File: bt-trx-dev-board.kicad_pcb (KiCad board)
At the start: 2 copper layers, 78 x 68 mm, 54 parts, among them J1 RJ45, J2 PTT_BUTTON, J3 AudioJack3, J4 ENAPLE_PTT_PULLUP, J5 PTT_SELECT, J6 I2C, J7 Conn_01x02, SW1 SW_Push, U1 SILabs_WT32i, U3 ESP32-DEVKIT

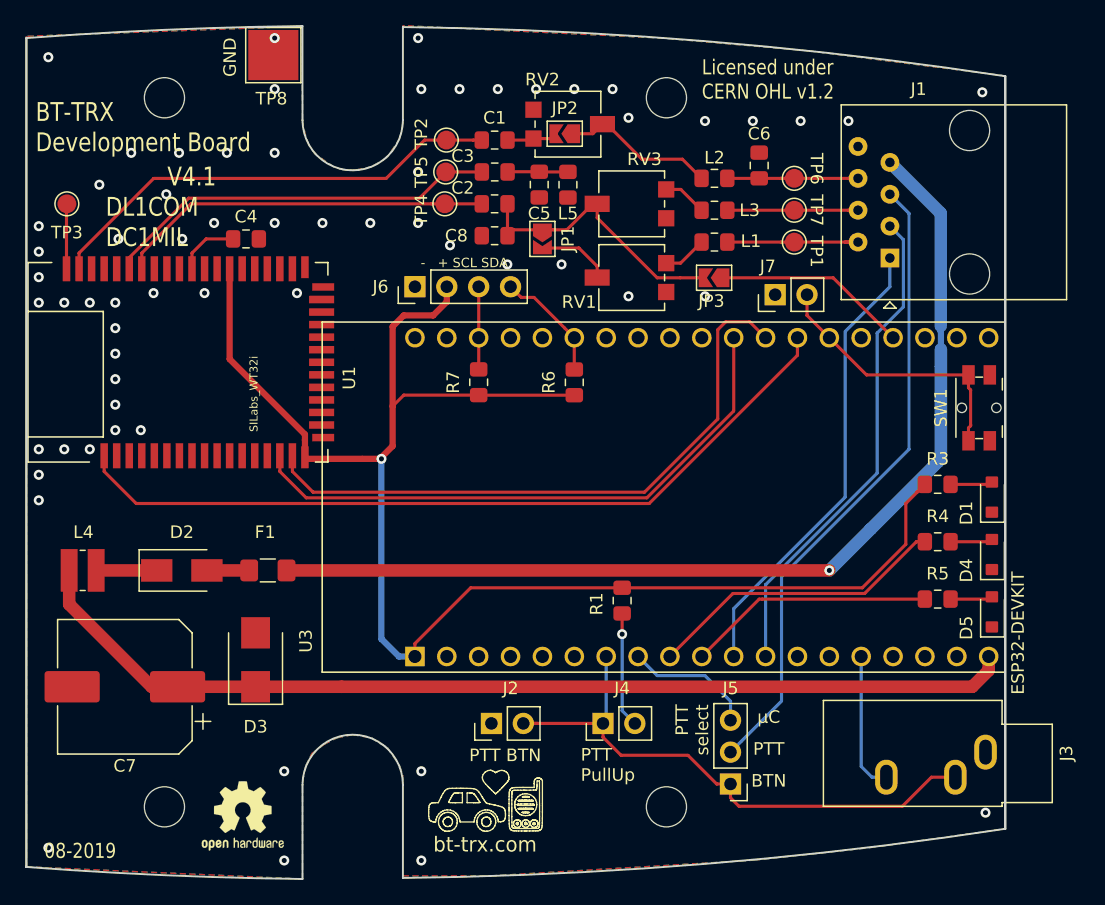
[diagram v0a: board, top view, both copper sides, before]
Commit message: Changed Silkscreen a bit
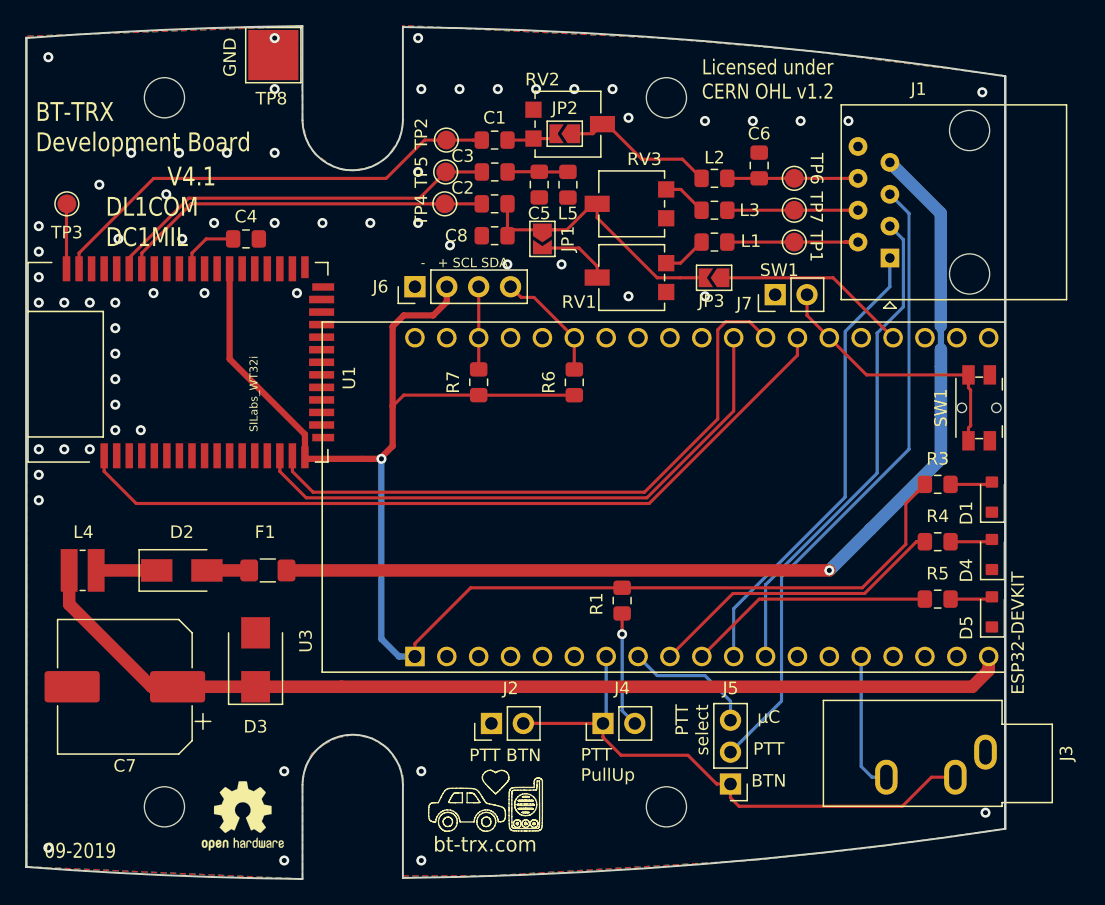
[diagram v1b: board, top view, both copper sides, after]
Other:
- board text added: "09-2019"
- board text added: "SW1"
- board text removed: "08-2019"
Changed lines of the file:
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@@
   (general
     (thickness 1.6)
-    (drawings 876)
+    (drawings 877)
     (tracks 275)
     (zones 0)
@@
     (tags "test point SMD pad")
     (attr virtual)
-    (fp_text reference TP1 (at 1.778 0.762 270 unlocked) (layer F.SilkS)
+    (fp_text reference TP1 (at 1.7526 0.3302 270 unlocked) (layer F.SilkS)
       (effects (font (size 1 1) (thickness 0.15)))
     )
@@
     (tags "test point SMD pad")
     (attr virtual)
-    (fp_text reference TP7 (at 1.778 0 270 unlocked) (layer F.SilkS)
+    (fp_text reference TP7 (at 1.7526 -0.2286 270 unlocked) (layer F.SilkS)
       (effects (font (size 1 1) (thickness 0.15)))
     )
@@
     (descr "Through hole straight pin header, 1x02, 2.54mm pitch, single row")
     (tags "Through hole pin header THT 1x02 2.54mm single row")
-    (fp_text reference J7 (at 2.2606 -0.5842 180) (layer F.SilkS)
+    (fp_text reference J7 (at -0.7112 -2.4638 180) (layer F.SilkS)
       (effects (font (size 1 1) (thickness 0.15)))
     )
@@
       ))
   )
+  (gr_text SW1 (at 178.8668 84.7852) (layer F.SilkS)
+    (effects (font (size 1 1) (thickness 0.15)) (justify left))
+  )
   (gr_text "-   + SCL SDA" (at 155.321 84.201) (layer F.SilkS)
     (effects (font (size 0.75 0.75) (thickness 0.125)))
@@
   (gr_line (start 154.4549 128.13161) (end 154.550279 128.21612) (layer F.SilkS) (width 0.09))
   (gr_line (start 153.416 128.27) (end 153.456692 128.22767) (layer F.SilkS) (width 0.09))
-  (gr_text 08-2019 (at 124.714 131.064) (layer F.SilkS)
+  (gr_text 09-2019 (at 124.714 131.064) (layer F.SilkS)
     (effects (font (size 1.2 1) (thickness 0.15)))
   )

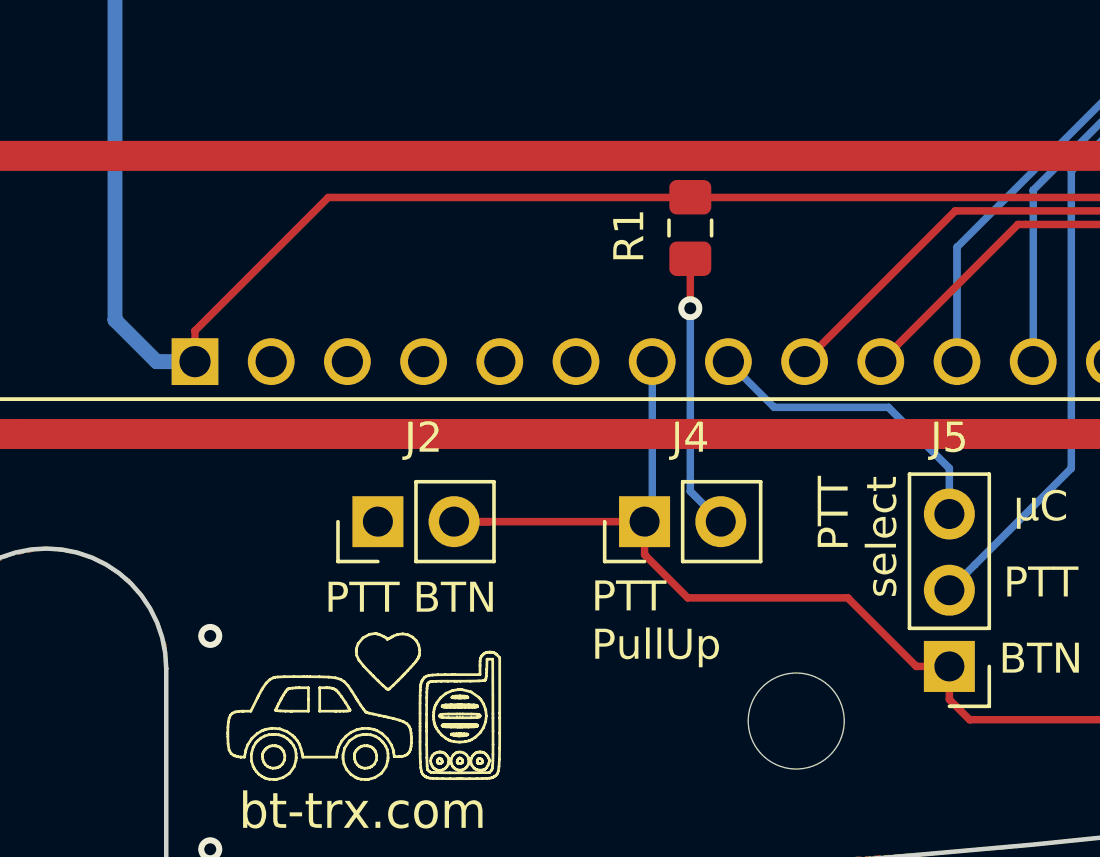
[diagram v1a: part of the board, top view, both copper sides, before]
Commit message: [#15] Replaced PTT Pullup Jumper wit Solder Jumper
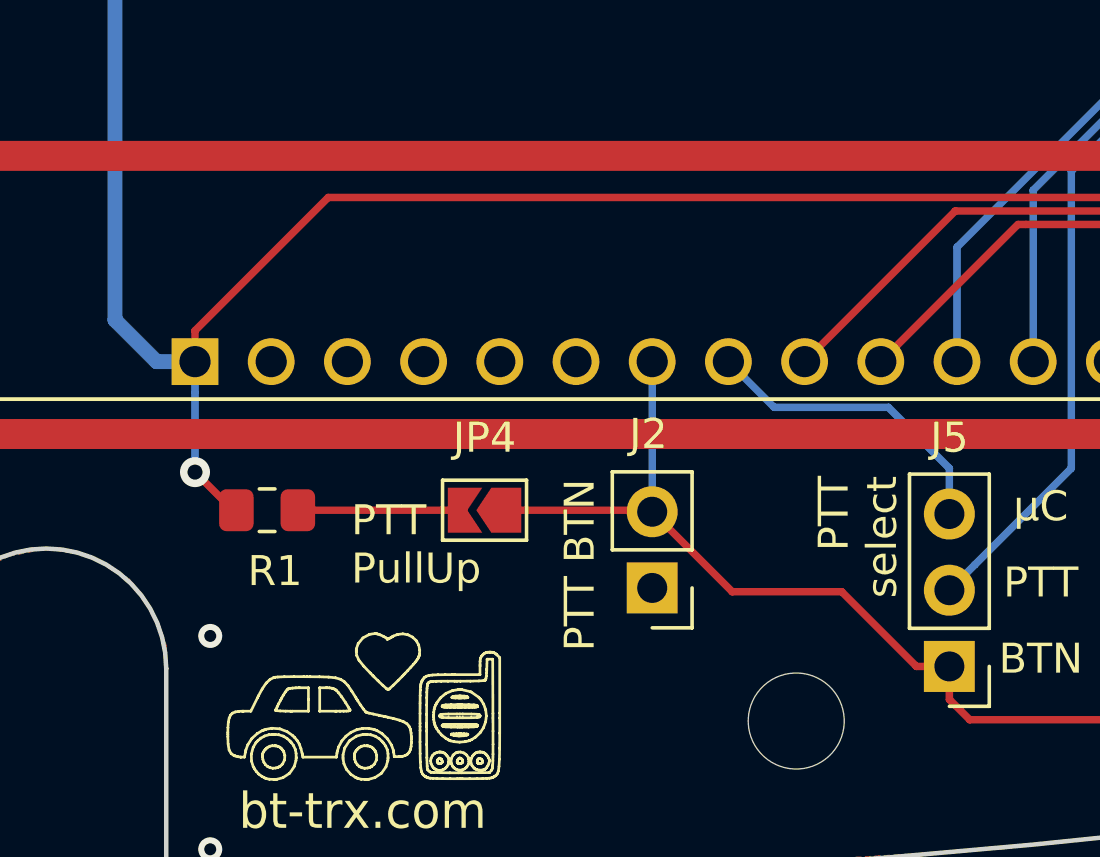
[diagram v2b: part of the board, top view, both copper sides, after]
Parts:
- removed J4: ENAPLE_PTT_PULLUP, Connector_PinHeader_2.54mm:PinHeader_1x02_P2.54mm_Vertical
- added JP4: EN_PTT_PULLUP, Jumper:SolderJumper-2_P1.3mm_Open_TrianglePad1.0x1.5mm, F.Cu at (161.0, 120.5)
- moved R1 17.0 mm to (153.8, 120.5), turned to 0 degrees
- moved J2 9.41 mm to (166.6, 123.1), turned to 180 degrees
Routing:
- net +3V3: track 122.1 -> 127.7 mm, vias 1 -> 2
- net /PTT_BUTTON: track 46.5 -> 42.2 mm
- net Net-(JP4-Pad2): track 9.18 -> 5.46 mm, vias 1 -> 0

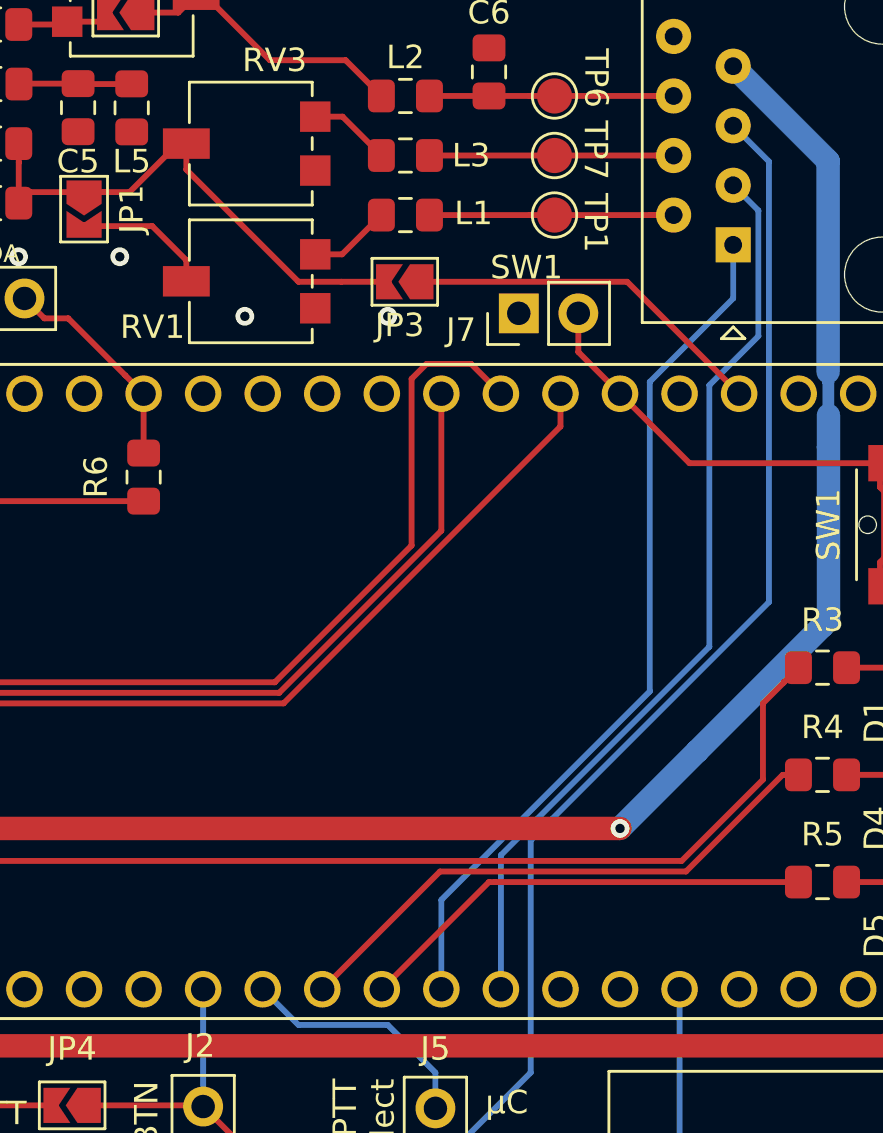
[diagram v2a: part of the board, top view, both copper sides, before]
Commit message: [#16] Move SW1 and VOX to usable Pins
* Moved SW1 form GPIO0 to GPIO18
* Added Pullup to SW1
* Moved VOX form GPIO2 to GPIO35
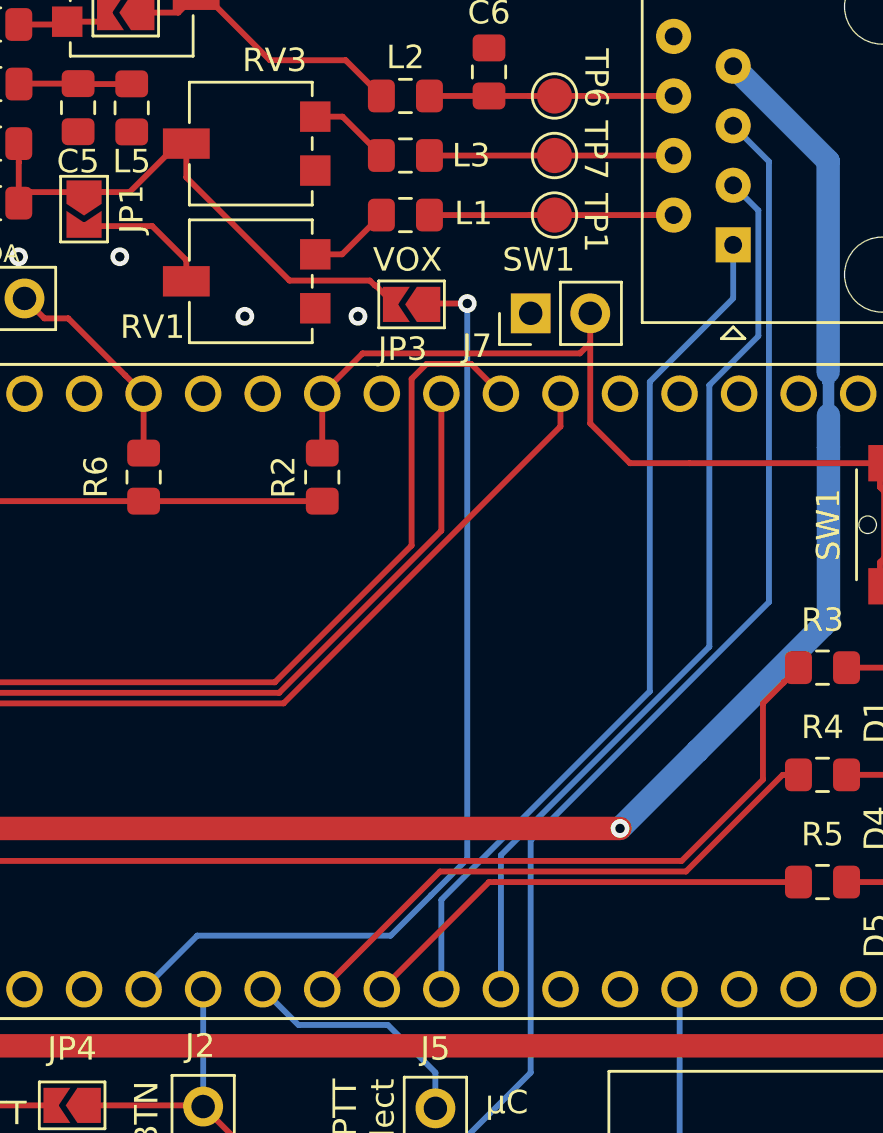
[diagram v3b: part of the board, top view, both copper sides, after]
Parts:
- added R2: 10k, Resistor_SMD:R_0805_2012Metric_Pad1.15x1.40mm_HandSolder, F.Cu at (171.7, 93.7)
- moved JP3 1.01 mm to (175.5, 86.4)
- moved J7 0.51 mm to (180.6, 86.7)
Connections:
- JP3 pad 1: Net-(JP3-Pad1) -> /Microcontroller/VOX
- U3 pad 28: (no net) -> /Microcontroller/BTN0
- U3 pad 33: /Microcontroller/BTN0 -> (no net)
- U3 pad 35: Net-(JP3-Pad1) -> (no net)
- U3 pad 6: (no net) -> /Microcontroller/VOX
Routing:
- net /Microcontroller/VOX: track 0.00 -> 41.5 mm, vias 0 -> 1
- net /Microcontroller/BTN0: track 21.6 -> 37.8 mm
- net Net-(JP3-Pad1): track 15.5 -> 0.00 mm
- net +3V3: track 127.7 -> 135.3 mm
- net AUDIO_B: track 22.4 -> 23.3 mm
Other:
- board text added: "VOX"

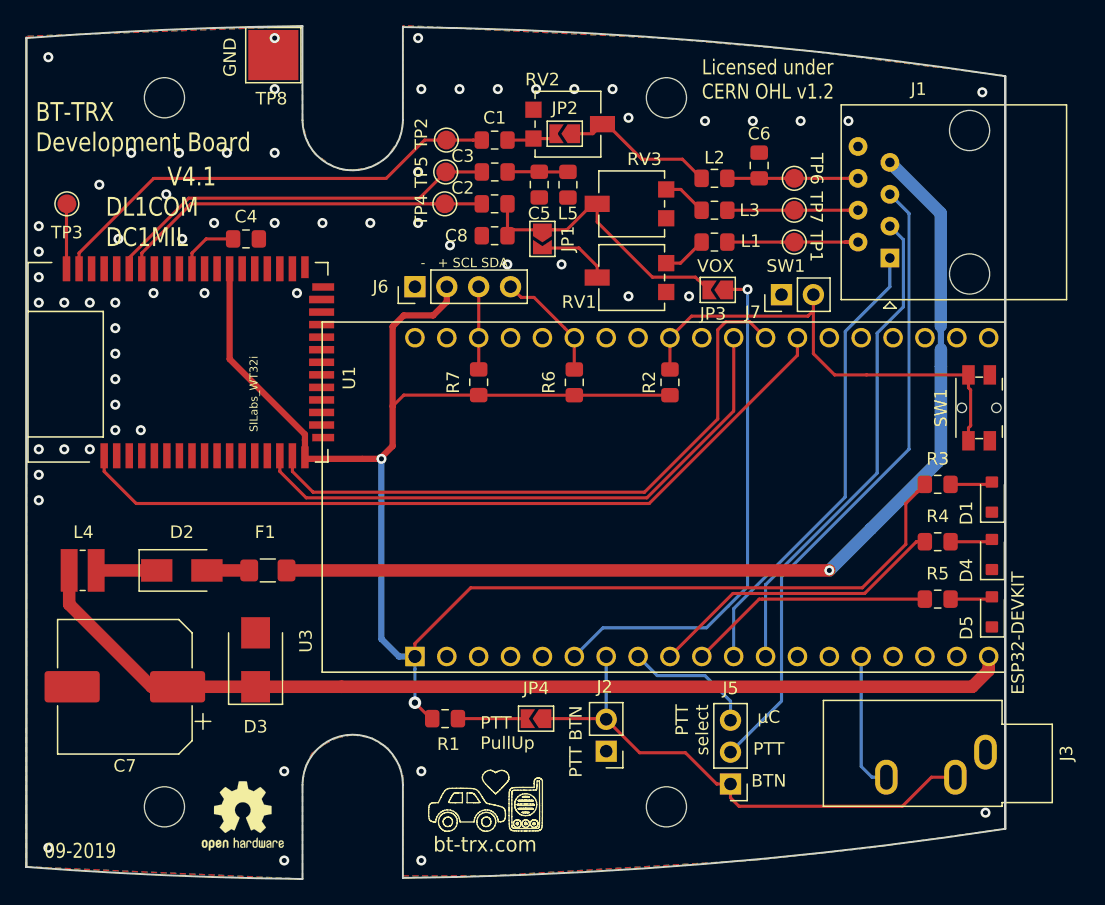
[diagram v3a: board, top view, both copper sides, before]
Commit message: Changed Silkscreen a bit
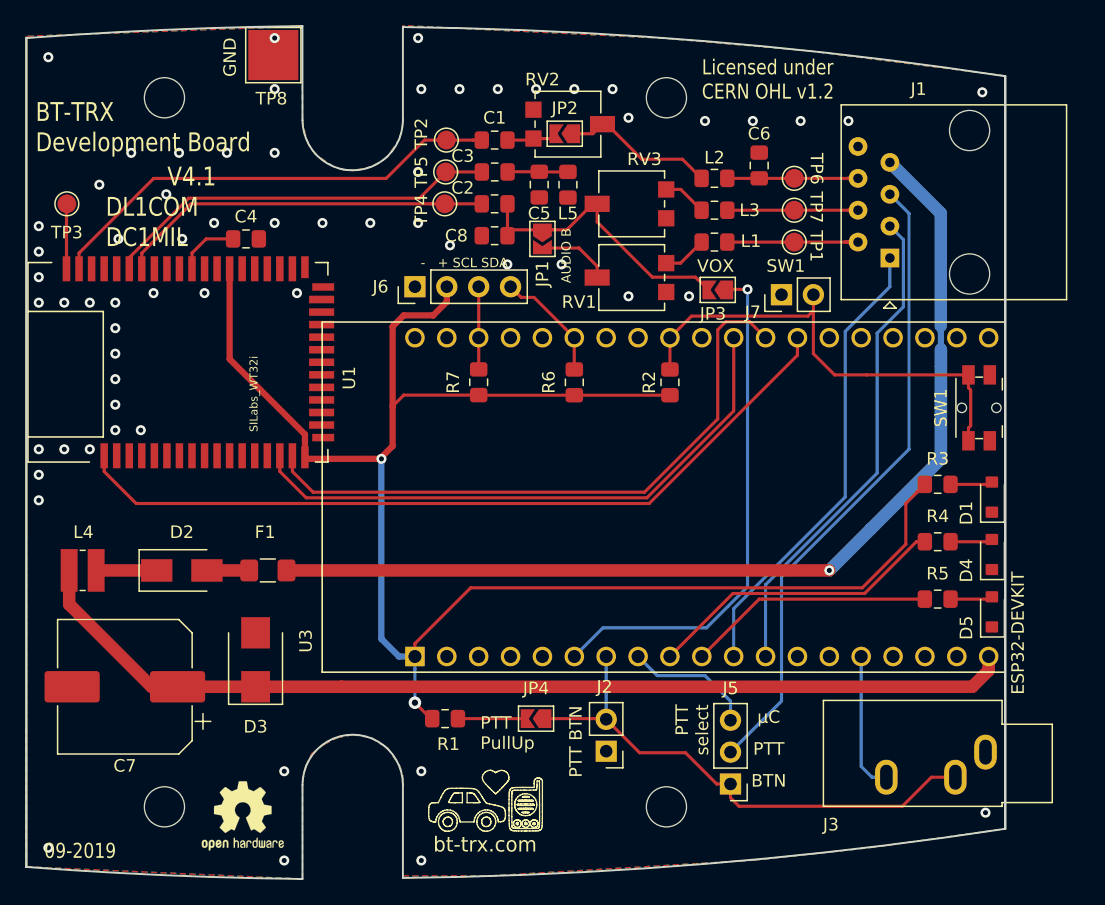
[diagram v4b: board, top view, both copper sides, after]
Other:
- board text added: "AUDIO B"
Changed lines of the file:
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@@
   (general
     (thickness 1.6)
-    (drawings 878)
+    (drawings 879)
     (tracks 290)
     (zones 0)
@@
   )
   (layers
-    (0 F.Cu signal hide)
+    (0 F.Cu signal)
     (31 B.Cu signal hide)
     (32 B.Adhes user)
@@
     (tags "solder jumper open")
     (attr virtual)
-    (fp_text reference JP1 (at 0 -2.032 90) (layer F.SilkS)
+    (fp_text reference JP1 (at 2.794 0 270) (layer F.SilkS)
       (effects (font (size 1 1) (thickness 0.15)))
     )
@@
       (effects (font (size 1 1) (thickness 0.15)))
     )
+    (fp_line (start 1.65 1.25) (end -1.65 1.25) (layer F.CrtYd) (width 0.05))
+    (fp_line (start 1.65 1.25) (end 1.65 -1.25) (layer F.CrtYd) (width 0.05))
+    (fp_line (start -1.65 -1.25) (end -1.65 1.25) (layer F.CrtYd) (width 0.05))
+    (fp_line (start -1.65 -1.25) (end 1.65 -1.25) (layer F.CrtYd) (width 0.05))
+    (fp_line (start -1.4 -1) (end 1.4 -1) (layer F.SilkS) (width 0.12))
+    (fp_line (start 1.4 -1) (end 1.4 1) (layer F.SilkS) (width 0.12))
+    (fp_line (start 1.4 1) (end -1.4 1) (layer F.SilkS) (width 0.12))
     (fp_line (start -1.4 1) (end -1.4 -1) (layer F.SilkS) (width 0.12))
-    (fp_line (start 1.4 1) (end -1.4 1) (layer F.SilkS) (width 0.12))
-    (fp_line (start 1.4 -1) (end 1.4 1) (layer F.SilkS) (width 0.12))
-    (fp_line (start -1.4 -1) (end 1.4 -1) (layer F.SilkS) (width 0.12))
-    (fp_line (start -1.65 -1.25) (end 1.65 -1.25) (layer F.CrtYd) (width 0.05))
-    (fp_line (start -1.65 -1.25) (end -1.65 1.25) (layer F.CrtYd) (width 0.05))
-    (fp_line (start 1.65 1.25) (end 1.65 -1.25) (layer F.CrtYd) (width 0.05))
-    (fp_line (start 1.65 1.25) (end -1.65 1.25) (layer F.CrtYd) (width 0.05))
+    (pad 1 smd custom (at -0.725 0 270) (size 0.3 0.3) (layers F.Cu F.Mask)
+      (net 15 AUDIO_B) (zone_connect 0)
+      (options (clearance outline) (anchor rect))
+      (primitives
+        (gr_poly (pts
+           (xy -0.5 -0.75) (xy 0.5 -0.75) (xy 1 0) (xy 0.5 0.75) (xy -0.5 0.75)
+) (width 0))
+      ))
     (pad 2 smd custom (at 0.725 0 270) (size 0.3 0.3) (layers F.Cu F.Mask)
       (net 31 "Net-(JP1-Pad2)") (zone_connect 0)
@@
         (gr_poly (pts
            (xy -0.65 -0.75) (xy 0.5 -0.75) (xy 0.5 0.75) (xy -0.65 0.75) (xy -0.15 0)
-) (width 0))
-      ))
-    (pad 1 smd custom (at -0.725 0 270) (size 0.3 0.3) (layers F.Cu F.Mask)
-      (net 15 AUDIO_B) (zone_connect 0)
-      (options (clearance outline) (anchor rect))
-      (primitives
-        (gr_poly (pts
-           (xy -0.5 -0.75) (xy 0.5 -0.75) (xy 1 0) (xy 0.5 0.75) (xy -0.5 0.75)
 ) (width 0))
       ))
@@
     (descr "TRS 3.5mm, horizontal, through-hole, https://www.cui.com/product/resource/sj1-353xng.pdf")
     (tags "TRS audio jack stereo horizontal")
-    (fp_text reference J3 (at 0.1 -6.45 90) (layer F.SilkS)
+    (fp_text reference J3 (at 5.7785 12.319 180) (layer F.SilkS)
       (effects (font (size 1 1) (thickness 0.15)))
     )
@@
     )
   )
+  (gr_text "AUDIO B" (at 163.449 83.6295 90) (layer F.SilkS)
+    (effects (font (size 0.75 0.75) (thickness 0.15)))
+  )
   (gr_text VOX (at 173.863 84.455) (layer F.SilkS)
